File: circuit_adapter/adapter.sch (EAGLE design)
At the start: 3 parts, among them CN1 5035521020, X1 2510-

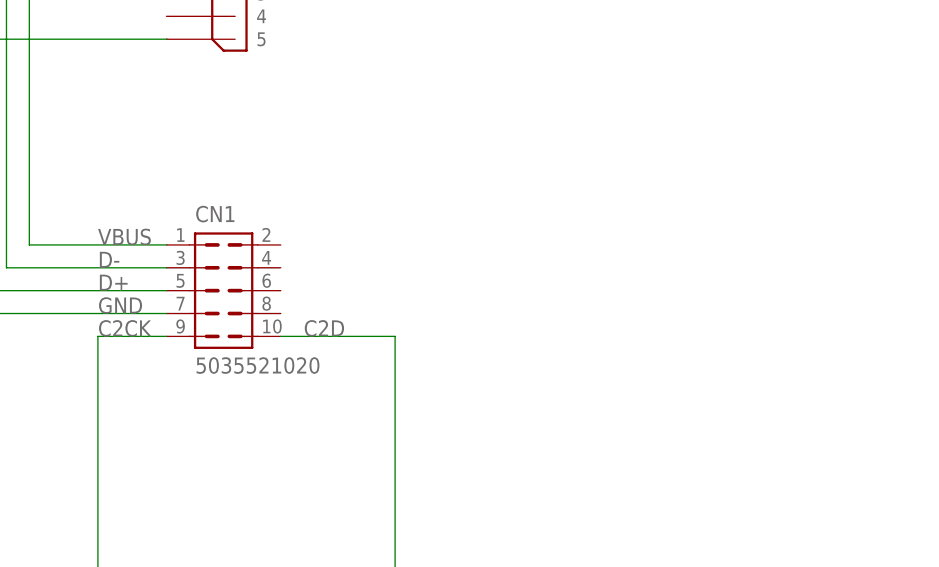
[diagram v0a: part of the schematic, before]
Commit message: Modified adapter circuit
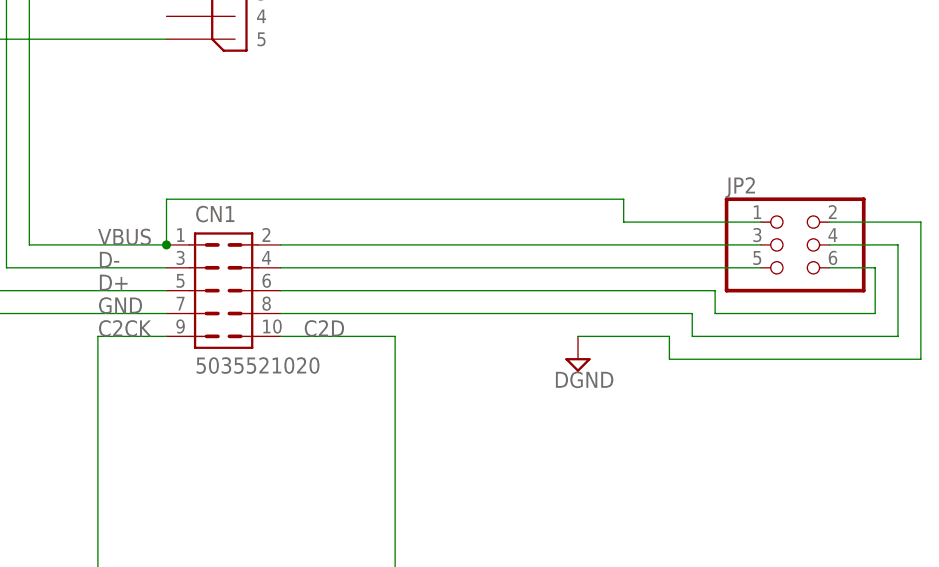
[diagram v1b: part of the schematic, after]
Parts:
- added JP2: (no value), pinhead:PINHD-2X3
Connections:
- new net N$1: CN1.2, JP2.3
- new net N$2: CN1.4, JP2.5
- new net N$3: CN1.6, JP2.6
- new net N$4: CN1.8, JP2.4
- net DGND: now also JP2.2
- net VBUS: now also JP2.1
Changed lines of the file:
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@@
 <part name="CN2" library="connector" deviceset="MICROUSB_ZX62D1-B-5PA(30)" device=""/>
 <part name="SUPPLY1" library="supply2" library_urn="urn:adsk.eagle:library:372" deviceset="DGND" device=""/>
+<part name="SUPPLY2" library="supply2" library_urn="urn:adsk.eagle:library:372" deviceset="DGND" device=""/>
+<part name="JP2" library="pinhead" library_urn="urn:adsk.eagle:library:325" deviceset="PINHD-2X3" device="" package3d_urn="urn:adsk.eagle:package:22462/2"/>
 </parts>
 <sheets>
@@
 <attribute name="VALUE" x="22.733" y="-8.255" size="1.778" layer="96"/>
 </instance>
+<instance part="SUPPLY2" gate="G$1" x="81.28" y="53.34">
+<attribute name="VALUE" x="78.613" y="50.165" size="1.778" layer="96"/>
+</instance>
+<instance part="JP2" gate="A" x="104.14" y="66.04">
+<attribute name="NAME" x="97.79" y="71.755" size="1.778" layer="95"/>
+<attribute name="VALUE" x="97.79" y="58.42" size="1.778" layer="96"/>
+</instance>
 </instances>
 <busses>
@@
 <junction x="25.4" y="20.32"/>
 </segment>
+<segment>
+<pinref part="SUPPLY2" gate="G$1" pin="DGND"/>
+<wire x1="91.44" y1="55.88" x2="81.28" y2="55.88" width="0.1524" layer="91"/>
+<pinref part="JP2" gate="A" pin="2"/>
+<wire x1="109.22" y1="68.58" x2="119.38" y2="68.58" width="0.1524" layer="91"/>
+<wire x1="119.38" y1="68.58" x2="119.38" y2="53.34" width="0.1524" layer="91"/>
+<wire x1="119.38" y1="53.34" x2="91.44" y2="53.34" width="0.1524" layer="91"/>
+<wire x1="91.44" y1="53.34" x2="91.44" y2="55.88" width="0.1524" layer="91"/>
+</segment>
 </net>
 <net name="VBUS" class="0">
@@
 <wire x1="20.32" y1="66.04" x2="35.56" y2="66.04" width="0.1524" layer="91"/>
 <label x="27.94" y="66.04" size="1.778" layer="95"/>
+<wire x1="35.56" y1="66.04" x2="35.56" y2="71.12" width="0.1524" layer="91"/>
+<junction x="35.56" y="66.04"/>
+<wire x1="35.56" y1="71.12" x2="86.36" y2="71.12" width="0.1524" layer="91"/>
+<wire x1="86.36" y1="71.12" x2="86.36" y2="68.58" width="0.1524" layer="91"/>
+<pinref part="JP2" gate="A" pin="1"/>
+<wire x1="86.36" y1="68.58" x2="101.6" y2="68.58" width="0.1524" layer="91"/>
 </segment>
 </net>
@@
 </segment>
 </net>
+<net name="N$1" class="1">
+<segment>
+<pinref part="CN1" gate="G$1" pin="2"/>
+<wire x1="48.26" y1="66.04" x2="101.6" y2="66.04" width="0.1524" layer="91"/>
+<pinref part="JP2" gate="A" pin="3"/>
+</segment>
+</net>
+<net name="N$2" class="1">
+<segment>
+<pinref part="CN1" gate="G$1" pin="4"/>
+<wire x1="101.6" y1="63.5" x2="48.26" y2="63.5" width="0.1524" layer="91"/>
+<pinref part="JP2" gate="A" pin="5"/>
+</segment>
+</net>
+<net name="N$3" class="1">
+<segment>
+<pinref part="CN1" gate="G$1" pin="6"/>
+<wire x1="48.26" y1="60.96" x2="96.52" y2="60.96" width="0.1524" layer="91"/>
+<wire x1="96.52" y1="60.96" x2="96.52" y2="58.42" width="0.1524" layer="91"/>
+<wire x1="96.52" y1="58.42" x2="114.3" y2="58.42" width="0.1524" layer="91"/>
+<wire x1="114.3" y1="58.42" x2="114.3" y2="63.5" width="0.1524" layer="91"/>
+<pinref part="JP2" gate="A" pin="6"/>
+<wire x1="114.3" y1="63.5" x2="109.22" y2="63.5" width="0.1524" layer="91"/>
+</segment>
+</net>
+<net name="N$4" class="1">
+<segment>
+<pinref part="CN1" gate="G$1" pin="8"/>
+<wire x1="93.98" y1="58.42" x2="48.26" y2="58.42" width="0.1524" layer="91"/>
+<wire x1="93.98" y1="58.42" x2="93.98" y2="55.88" width="0.1524" layer="91"/>
+<wire x1="93.98" y1="55.88" x2="116.84" y2="55.88" width="0.1524" layer="91"/>
+<wire x1="116.84" y1="55.88" x2="116.84" y2="66.04" width="0.1524" layer="91"/>
+<pinref part="JP2" gate="A" pin="4"/>
+<wire x1="116.84" y1="66.04" x2="109.22" y2="66.04" width="0.1524" layer="91"/>
+</segment>
+</net>

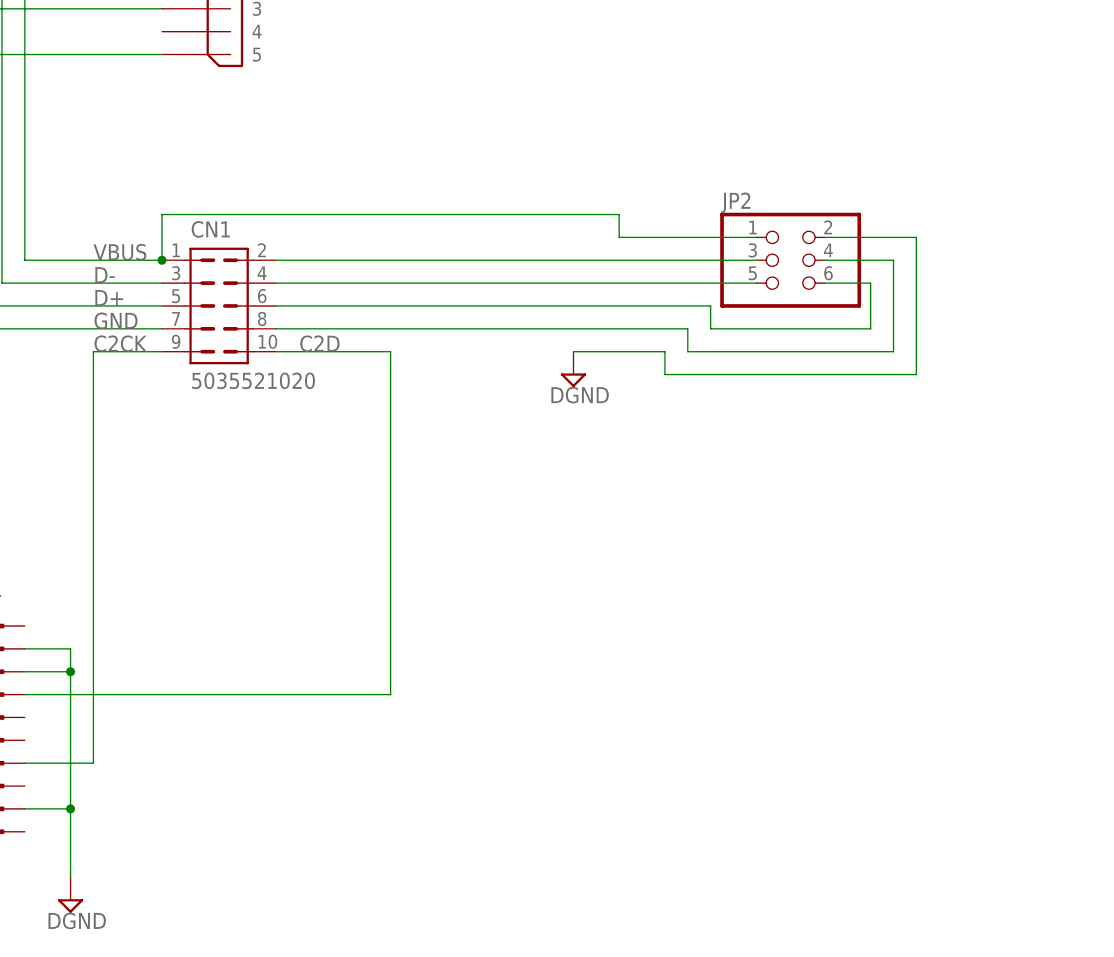
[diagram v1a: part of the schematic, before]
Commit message: Modified adapter circuit
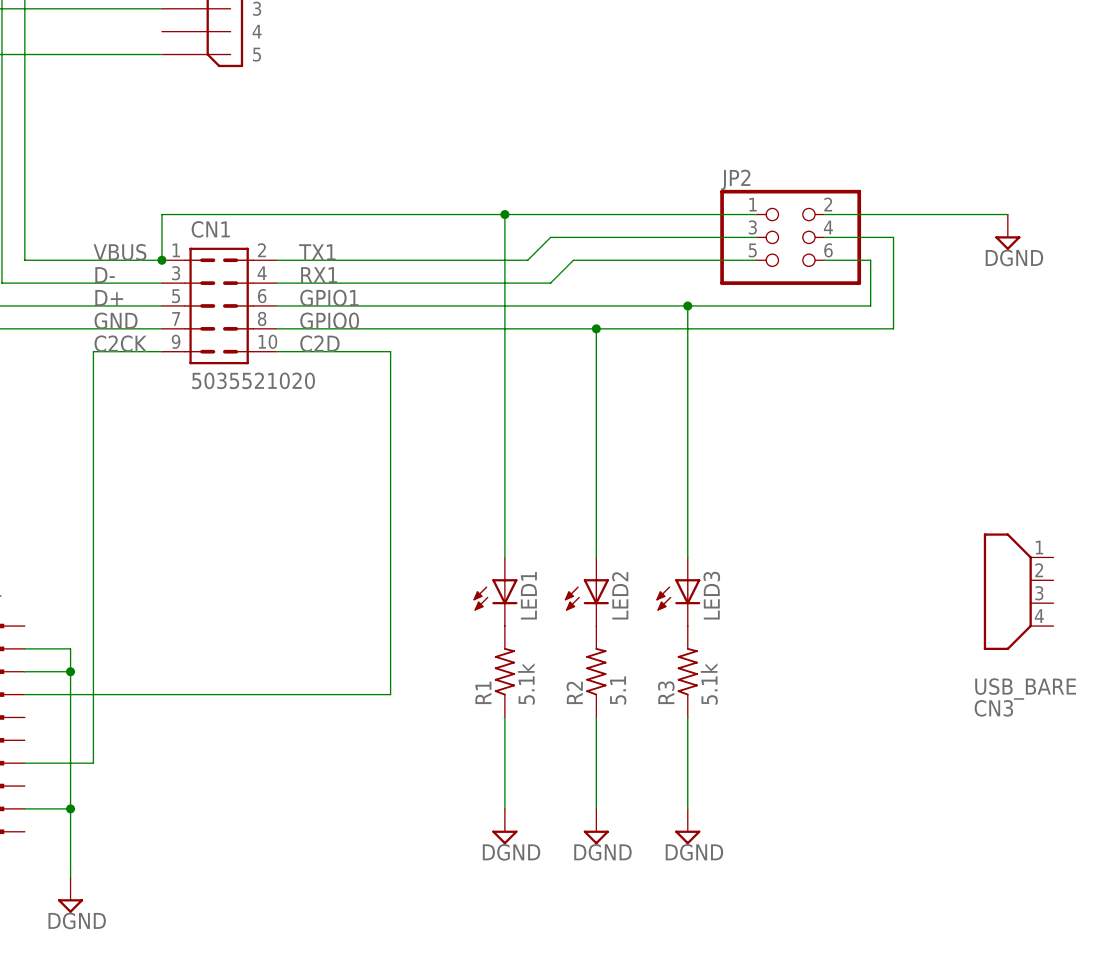
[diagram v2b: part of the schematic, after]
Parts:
- added CN3: USB_BARE, connector:USB_BARE
- added LED1, LED2, LED3: (no value), led:LEDSML0603
- added R1, R3: 5.1k, rcl:R-US_R0402
- added R2: 5.1, rcl:R-US_R0402
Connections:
- net N$1 renamed TX1
- net N$2 renamed RX1
- removed net DGND: JP2.2, X1-2.KL, X1-3.KL, X1-9.KL
- removed net N$4: CN1.8, JP2.4
- new net GPIO0: CN1.8, JP2.4, LED2.A
- new net GPIO1: CN1.6, JP2.6, LED3.A
- new net N$1: LED1.C, R1.2
- new net N$2: LED2.C, R2.2
- net GND: now also JP2.2, R1.1, R2.1, R3.1, X1-2.KL, X1-3.KL, X1-9.KL
- net N$3: now also LED3.C, R3.2; no longer CN1.6, JP2.6
- net VBUS: now also LED1.A
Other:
- moved on the sheet: JP2
